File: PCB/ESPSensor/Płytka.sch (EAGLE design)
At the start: 50 parts, among them IC2 LM2576S/5V, J1 HUM1, J2 HUM2, J3 TEMP, J4 SUN, Q4 BSS138, Q5 BSS138, U1 ESP-WROOM-32, U2 LM3940IMP-3.3

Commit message: no message
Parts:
- added SV1, SV3, SV4, SV5: (no value), con-lstb:MA04-1
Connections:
- removed net P1ON: U1.IO19
- removed net P2ON: U1.IO18
- net +3V3: now also J3.1, J4.1
- net +5V: no longer J3.1, J4.1
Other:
- moved on the sheet: Q4, Q5, R14, R15, R16, R25, R27, R28, R29, SV2

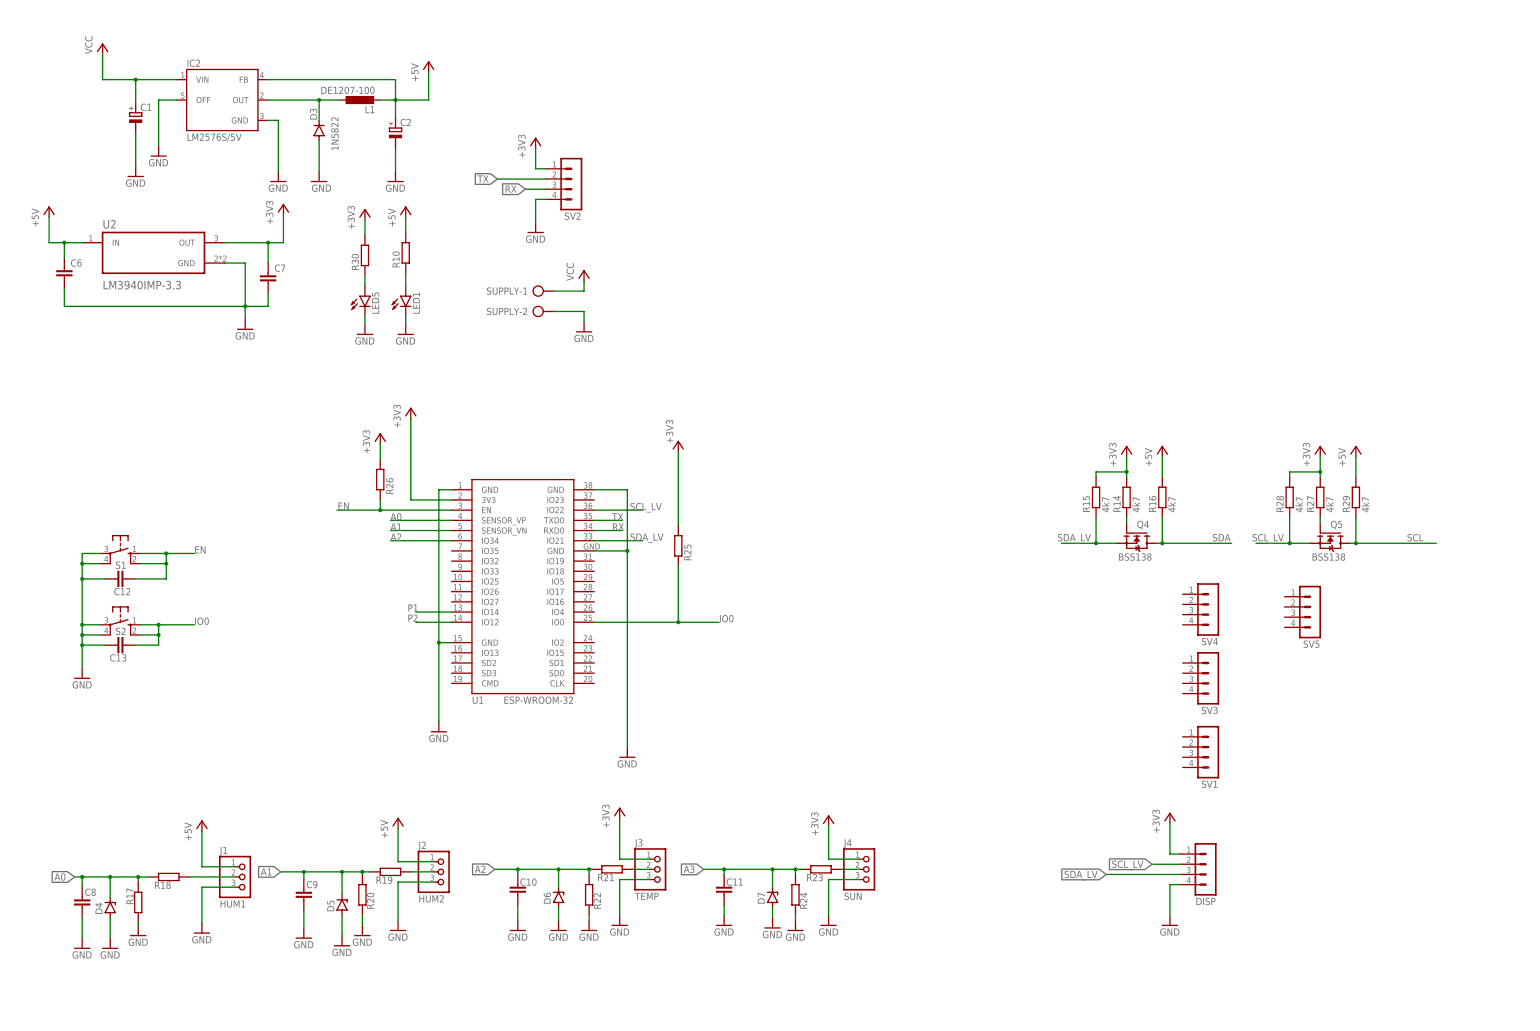
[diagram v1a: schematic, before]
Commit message: Add new PCBs
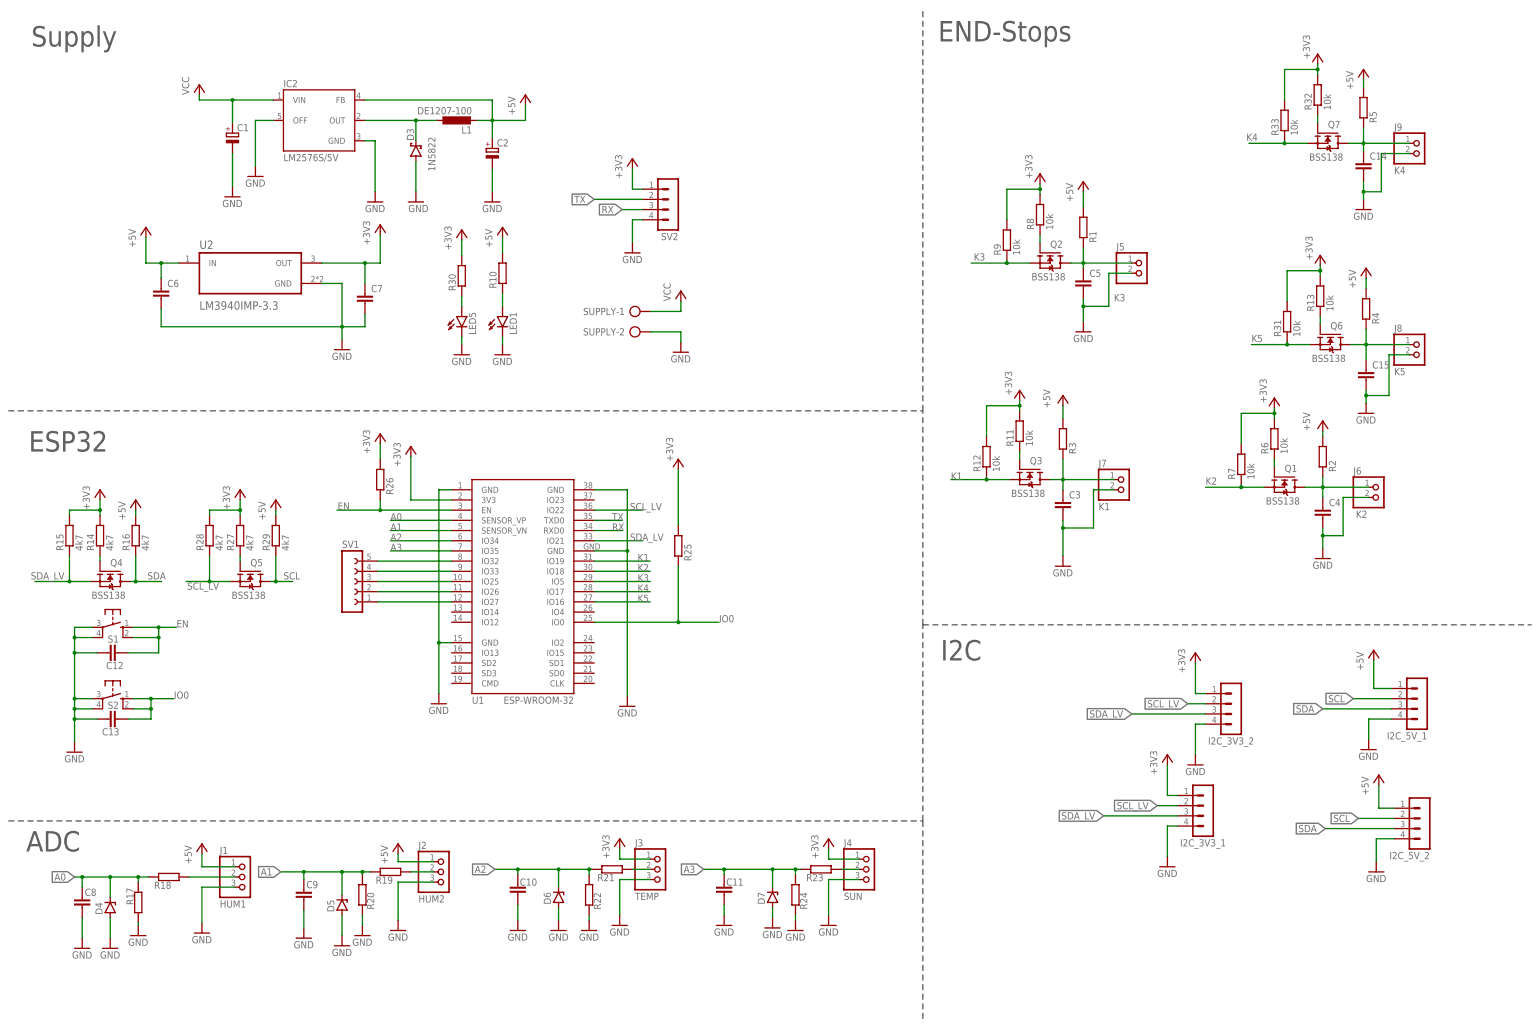
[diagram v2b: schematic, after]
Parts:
- removed DISP, SV3, SV4, SV5: (no value), con-lstb:MA04-1
- added C14, C15, C3, C4, C5: (no value), rcl:C-EUC0805K
- added I2C_3V3_1, I2C_3V3_2, I2C_5V_1, I2C_5V_2: (no value), con-lstb:MA04-1
- added J5: K3, PUTRocketLab_connectors:WT-2MM-2PINSTRAIGHT
- added J6: K2, PUTRocketLab_connectors:WT-2MM-2PINSTRAIGHT
- added J7: K1, PUTRocketLab_connectors:WT-2MM-2PINSTRAIGHT
- added J8: K5, PUTRocketLab_connectors:WT-2MM-2PINSTRAIGHT
- added J9: K4, PUTRocketLab_connectors:WT-2MM-2PINSTRAIGHT
- added Q1, Q2, Q3, Q6, Q7: BSS138, bss138_10:BSS138
- added R1, R2, R3, R4, R5: (no value), rcl:R-EU_R0805
- added R11, R12, R13, R31, R32, R33, R6, R7, R8, R9: 10k, rcl:R-EU_R0805
- C2: device rcl:CPOL-EUE2.5-6 -> rcl:CPOL-EUE3.5-8
- D3: device diode:1N4004 -> diode:1N5908
- IC2: device v-reg-3:LM2576S -> v-reg-3:LM2576T
- SV1: device con-lstb:MA04-1 -> con-lsta:FE05-1
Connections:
- removed net P1: U1.IO14
- removed net P2: U1.IO12
- new net K1: Q3.S, R12.1, U1.IO19
- new net K2: Q1.S, R7.1, U1.IO18
- new net K3: Q2.S, R9.1, U1.IO5
- new net K4: Q7.S, R33.1, U1.IO17
- new net K5: Q6.S, R31.1, U1.IO16
- new net N$1: C5.1, J5.1, Q2.D, R1.1
- new net N$10: SV1.5, U1.IO32
- new net N$11: Q1.G, R6.1
- new net N$12: SV1.4, U1.IO33
- new net N$13: Q2.G, R8.1
- new net N$14: SV1.3, U1.IO25
- new net N$16: Q3.G, R11.1
- new net N$17: SV1.2, U1.IO26
- new net N$2: C4.1, J6.1, Q1.D, R2.1
- new net N$20: Q6.G, R13.1
- new net N$22: SV1.1, U1.IO27
- new net N$24: Q7.G, R32.1
- new net N$5: C3.1, J7.1, Q3.D, R3.1
- new net N$6: C14.1, J9.1, Q7.D, R5.1
- new net N$7: C15.1, J8.1, Q6.D, R4.1
- net +3V3: now also I2C_3V3_1.1, I2C_3V3_2.1, R11.2, R12.2, R13.2, R31.2, R32.2, R33.2, R6.2, R7.2, R8.2, R9.2
- net +5V: now also I2C_5V_1.1, I2C_5V_2.1, R1.2, R2.2, R3.2, R4.2, R5.2; no longer DISP.1
- net A3: now also U1.IO35
- net GND: now also C14.2, C15.2, C3.2, C4.2, C5.2, I2C_3V3_1.4, I2C_3V3_2.4, I2C_5V_1.4, I2C_5V_2.4, J5.2, J6.2, J7.2, J8.2, J9.2; no longer DISP.4
- net SCL: now also I2C_5V_1.2, I2C_5V_2.2
- net SCL_LV: now also I2C_3V3_1.2, I2C_3V3_2.2; no longer DISP.2
- net SDA: now also I2C_5V_1.3, I2C_5V_2.3
- net SDA_LV: now also I2C_3V3_1.3, I2C_3V3_2.3; no longer DISP.3
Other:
- note added: "ADC"
- note added: "END-Stops"
- note added: "ESP32"
- note added: "I2C"
- note added: "Supply"
- moved on the sheet: C1, C12, C13, C2, C6, C7, IC2, L1, LED1, LED5, Q4, Q5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

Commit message: Creating charts
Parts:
- C1, C6: value (none) -> 100u
- C14, C15, C2, C3, C4, C5, C7: value (none) -> 10u
- R10: value (none) -> 330
- R17, R20: value (none) -> 20K
- R18, R19: value (none) -> 10K
- R30: value (none) -> 100
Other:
- note added: "ESP Sensors"
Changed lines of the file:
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@@
 <part name="GND7" library="supply1" library_urn="urn:adsk.eagle:library:371" deviceset="GND" device=""/>
 <part name="IC2" library="v-reg-3" deviceset="LM2576" device="T" value="LM2576S/5V"/>
-<part name="C1" library="rcl" library_urn="urn:adsk.eagle:library:334" deviceset="CPOL-EU" device="E2.5-6" package3d_urn="urn:adsk.eagle:package:23349/1"/>
-<part name="C2" library="rcl" library_urn="urn:adsk.eagle:library:334" deviceset="CPOL-EU" device="E3.5-8" package3d_urn="urn:adsk.eagle:package:23360/2"/>
+<part name="C1" library="rcl" library_urn="urn:adsk.eagle:library:334" deviceset="CPOL-EU" device="E2.5-6" package3d_urn="urn:adsk.eagle:package:23349/1" value="100u"/>
+<part name="C2" library="rcl" library_urn="urn:adsk.eagle:library:334" deviceset="CPOL-EU" device="E3.5-8" package3d_urn="urn:adsk.eagle:package:23360/2" value="10u"/>
 <part name="D3" library="diode" library_urn="urn:adsk.eagle:library:210" deviceset="1N5908" device="" package3d_urn="urn:adsk.eagle:package:43355/2" value="1N5822"/>
 <part name="GND13" library="supply1" library_urn="urn:adsk.eagle:library:371" deviceset="GND" device=""/>
@@
 <part name="LED1" library="led" library_urn="urn:adsk.eagle:library:259" deviceset="LED" device="SML0805" package3d_urn="urn:adsk.eagle:package:15830/1"/>
 <part name="GND21" library="supply1" library_urn="urn:adsk.eagle:library:371" deviceset="GND" device=""/>
-<part name="R10" library="rcl" library_urn="urn:adsk.eagle:library:334" deviceset="R-EU_" device="R0805" package3d_urn="urn:adsk.eagle:package:23553/2"/>
+<part name="R10" library="rcl" library_urn="urn:adsk.eagle:library:334" deviceset="R-EU_" device="R0805" package3d_urn="urn:adsk.eagle:package:23553/2" value="330"/>
 <part name="P+19" library="supply1" library_urn="urn:adsk.eagle:library:371" deviceset="+5V" device=""/>
 <part name="L1" library="ferrocore" deviceset="DE1207-100" device=""/>
@@
 <part name="P+28" library="supply1" library_urn="urn:adsk.eagle:library:371" deviceset="+5V" device=""/>
 <part name="GND28" library="supply1" library_urn="urn:adsk.eagle:library:371" deviceset="GND" device=""/>
-<part name="C6" library="rcl" library_urn="urn:adsk.eagle:library:334" deviceset="C-EU" device="C0805K" package3d_urn="urn:adsk.eagle:package:23681/2"/>
-<part name="C7" library="rcl" library_urn="urn:adsk.eagle:library:334" deviceset="C-EU" device="C0805K" package3d_urn="urn:adsk.eagle:package:23681/2"/>
+<part name="C6" library="rcl" library_urn="urn:adsk.eagle:library:334" deviceset="C-EU" device="C0805K" package3d_urn="urn:adsk.eagle:package:23681/2" value="100u"/>
+<part name="C7" library="rcl" library_urn="urn:adsk.eagle:library:334" deviceset="C-EU" device="C0805K" package3d_urn="urn:adsk.eagle:package:23681/2" value="10u"/>
 <part name="+3V3" library="supply1" library_urn="urn:adsk.eagle:library:371" deviceset="+3V3" device=""/>
-<part name="R30" library="rcl" library_urn="urn:adsk.eagle:library:334" deviceset="R-EU_" device="R0805" package3d_urn="urn:adsk.eagle:package:23553/2"/>
+<part name="R30" library="rcl" library_urn="urn:adsk.eagle:library:334" deviceset="R-EU_" device="R0805" package3d_urn="urn:adsk.eagle:package:23553/2" value="100"/>
 <part name="LED5" library="led" library_urn="urn:adsk.eagle:library:259" deviceset="LED" device="SML0805" package3d_urn="urn:adsk.eagle:package:15830/1"/>
 <part name="GND29" library="supply1" library_urn="urn:adsk.eagle:library:371" deviceset="GND" device=""/>
@@
 <part name="J3" library="PUTRocketLab_connectors" deviceset="WT-2MM-3PIN" device="STRAIGHT" value="TEMP"/>
 <part name="J4" library="PUTRocketLab_connectors" deviceset="WT-2MM-3PIN" device="STRAIGHT" value="SUN"/>
-<part name="R17" library="rcl" library_urn="urn:adsk.eagle:library:334" deviceset="R-EU_" device="R0805" package3d_urn="urn:adsk.eagle:package:23553/2"/>
-<part name="R18" library="rcl" library_urn="urn:adsk.eagle:library:334" deviceset="R-EU_" device="R0805" package3d_urn="urn:adsk.eagle:package:23553/2"/>
+<part name="R17" library="rcl" library_urn="urn:adsk.eagle:library:334" deviceset="R-EU_" device="R0805" package3d_urn="urn:adsk.eagle:package:23553/2" value="20K"/>
+<part name="R18" library="rcl" library_urn="urn:adsk.eagle:library:334" deviceset="R-EU_" device="R0805" package3d_urn="urn:adsk.eagle:package:23553/2" value="10K"/>
 <part name="GND1" library="supply1" library_urn="urn:adsk.eagle:library:371" deviceset="GND" device=""/>
-<part name="R19" library="rcl" library_urn="urn:adsk.eagle:library:334" deviceset="R-EU_" device="R0805" package3d_urn="urn:adsk.eagle:package:23553/2"/>
-<part name="R20" library="rcl" library_urn="urn:adsk.eagle:library:334" deviceset="R-EU_" device="R0805" package3d_urn="urn:adsk.eagle:package:23553/2"/>
+<part name="R19" library="rcl" library_urn="urn:adsk.eagle:library:334" deviceset="R-EU_" device="R0805" package3d_urn="urn:adsk.eagle:package:23553/2" value="10K"/>
+<part name="R20" library="rcl" library_urn="urn:adsk.eagle:library:334" deviceset="R-EU_" device="R0805" package3d_urn="urn:adsk.eagle:package:23553/2" value="20K"/>
 <part name="R21" library="rcl" library_urn="urn:adsk.eagle:library:334" deviceset="R-EU_" device="R0805" package3d_urn="urn:adsk.eagle:package:23553/2"/>
 <part name="R22" library="rcl" library_urn="urn:adsk.eagle:library:334" deviceset="R-EU_" device="R0805" package3d_urn="urn:adsk.eagle:package:23553/2"/>
@@
 <part name="J8" library="PUTRocketLab_connectors" deviceset="WT-2MM-2PIN" device="STRAIGHT" value="K5"/>
 <part name="J9" library="PUTRocketLab_connectors" deviceset="WT-2MM-2PIN" device="STRAIGHT" value="K4"/>
-<part name="C3" library="rcl" library_urn="urn:adsk.eagle:library:334" deviceset="C-EU" device="C0805K" package3d_urn="urn:adsk.eagle:package:23681/2"/>
-<part name="C4" library="rcl" library_urn="urn:adsk.eagle:library:334" deviceset="C-EU" device="C0805K" package3d_urn="urn:adsk.eagle:package:23681/2"/>
-<part name="C5" library="rcl" library_urn="urn:adsk.eagle:library:334" deviceset="C-EU" device="C0805K" package3d_urn="urn:adsk.eagle:package:23681/2"/>
-<part name="C14" library="rcl" library_urn="urn:adsk.eagle:library:334" deviceset="C-EU" device="C0805K" package3d_urn="urn:adsk.eagle:package:23681/2"/>
-<part name="C15" library="rcl" library_urn="urn:adsk.eagle:library:334" deviceset="C-EU" device="C0805K" package3d_urn="urn:adsk.eagle:package:23681/2"/>
+<part name="C3" library="rcl" library_urn="urn:adsk.eagle:library:334" deviceset="C-EU" device="C0805K" package3d_urn="urn:adsk.eagle:package:23681/2" value="10u"/>
+<part name="C4" library="rcl" library_urn="urn:adsk.eagle:library:334" deviceset="C-EU" device="C0805K" package3d_urn="urn:adsk.eagle:package:23681/2" value="10u"/>
+<part name="C5" library="rcl" library_urn="urn:adsk.eagle:library:334" deviceset="C-EU" device="C0805K" package3d_urn="urn:adsk.eagle:package:23681/2" value="10u"/>
+<part name="C14" library="rcl" library_urn="urn:adsk.eagle:library:334" deviceset="C-EU" device="C0805K" package3d_urn="urn:adsk.eagle:package:23681/2" value="10u"/>
+<part name="C15" library="rcl" library_urn="urn:adsk.eagle:library:334" deviceset="C-EU" device="C0805K" package3d_urn="urn:adsk.eagle:package:23681/2" value="10u"/>
 <part name="GND10" library="supply1" library_urn="urn:adsk.eagle:library:371" deviceset="GND" device=""/>
 <part name="GND11" library="supply1" library_urn="urn:adsk.eagle:library:371" deviceset="GND" device=""/>
@@
 <text x="236.22" y="93.98" size="5.08" layer="97">I2C</text>
 <text x="235.585" y="248.285" size="5.08" layer="97">END-Stops</text>
+<text x="344.17" y="15.494" size="2.1844" layer="94">ESP Sensors</text>
 </plain>
 <instances>
@@
 <instance part="C1" gate="G$1" x="59.69" y="225.425" smashed="yes">
 <attribute name="NAME" x="60.833" y="225.9076" size="1.778" layer="95"/>
-<attribute name="VALUE" x="60.833" y="220.8276" size="1.778" layer="96"/>
+<attribute name="VALUE" x="52.578" y="219.5576" size="1.778" layer="96"/>
 </instance>
 <instance part="C2" gate="G$1" x="124.46" y="221.615" smashed="yes">
@@
 </instance>
 <instance part="FRAME1" gate="G$1" x="0" y="0" smashed="yes">
-<attribute name="DRAWING_NAME" x="344.17" y="15.24" size="2.54" layer="94"/>
 <attribute name="LAST_DATE_TIME" x="344.17" y="10.16" size="2.286" layer="94"/>
 <attribute name="SHEET" x="357.505" y="5.08" size="2.54" layer="94"/>
@@
 <instance part="R17" gate="G$1" x="36.195" y="33.655" smashed="yes" rot="MR90">
 <attribute name="NAME" x="33.2486" y="33.02" size="1.778" layer="95" rot="MR90"/>
-<attribute name="VALUE" x="32.893" y="29.845" size="1.778" layer="96" rot="MR90"/>
+<attribute name="VALUE" x="37.973" y="31.75" size="1.778" layer="96" rot="MR90"/>
 </instance>
 <instance part="R18" gate="G$1" x="43.815" y="40.005" smashed="yes" rot="MR0">
 <attribute name="NAME" x="44.45" y="37.0586" size="1.778" layer="95" rot="MR0"/>
-<attribute name="VALUE" x="47.625" y="36.703" size="1.778" layer="96" rot="MR0"/>
+<attribute name="VALUE" x="45.085" y="41.783" size="1.778" layer="96" rot="MR0"/>
 </instance>
 <instance part="GND1" gate="1" x="36.195" y="25.4" smashed="yes">
@@
 <instance part="R19" gate="G$1" x="99.06" y="41.275" smashed="yes" rot="MR0">
 <attribute name="NAME" x="99.695" y="38.3286" size="1.778" layer="95" rot="MR0"/>
-<attribute name="VALUE" x="102.87" y="37.973" size="1.778" layer="96" rot="MR0"/>
+<attribute name="VALUE" x="99.695" y="36.068" size="1.778" layer="96" rot="MR0"/>
 </instance>
 <instance part="R20" gate="G$1" x="92.075" y="35.56" smashed="yes" rot="MR270">
-<attribute name="NAME" x="95.0214" y="36.195" size="1.778" layer="95" rot="MR270"/>
-<attribute name="VALUE" x="95.377" y="39.37" size="1.778" layer="96" rot="MR270"/>
+<attribute name="NAME" x="90.5764" y="37.465" size="1.778" layer="95" rot="MR270"/>
+<attribute name="VALUE" x="94.742" y="37.465" size="1.778" layer="96" rot="MR270"/>
 </instance>
 <instance part="R21" gate="G$1" x="154.305" y="41.91" smashed="yes" rot="MR0">
